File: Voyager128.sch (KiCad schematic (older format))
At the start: 22 parts, among them J1 AppleIIBus, U1 74HCT245, U2 621024, U3 GAL22V10, U4 74AHCT125

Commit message: Board done but ugly
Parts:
- removed U2: 621024, stdpads:SOP-32_P1.27mm, symbol GW_RAM:SRAM-128Kx8-SOP-32
- removed U3: GAL22V10, stdpads:PLCC-28, symbol GW_PLD:GAL22V10-PLCC
- removed U4: 74AHCT125, stdpads:SOIC-14_3.9mm, symbol 74xx:74LS125
- added C10, C11, C12, C13, C14, C15, C16, C7, C8, C9: 2u2, stdpads:C_0603, symbol Device:C_Small
- added U1: 621024, stdpads:TSOP-I-32_18.4x8mm_P0.5mm, symbol GW_RAM:SRAM-128Kx8-TSOP1-32
- added U10: 74LS32, stdpads:TSSOP-14_4.4x5mm_P0.65mm, symbol 74xx:74LS32
- added U11: 74AHC1G126GW, stdpads:SOT-353, symbol GW_Logic:741G126GW
- added U3, U4: 74LS174, stdpads:TSSOP-16_4.4x5mm_P0.65mm, symbol 74xx:74LS174
- added U5: 74LS04, stdpads:TSSOP-14_4.4x5mm_P0.65mm, symbol 74xx:74LS04
- added U6, U7, U8, U9: 74LS08, stdpads:TSSOP-14_4.4x5mm_P0.65mm, symbol 74xx:74LS08
- C2, C3, C4, C6: footprint stdpads:C_0805 -> stdpads:C_0603
- R1: value 1k -> 3k3
- U2: renamed from U1; footprint stdpads:SOIC-20W_7.5mm -> stdpads:TSSOP-20_4.4x6.5mm_P0.65mm
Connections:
- net labels added: ENWR1A0, INHOE, RCS, ~A0XOR1~, ~DEV~andA2, ~DEV~and~A2~
- net labels removed: R~CS~1, ~INH~b
- wire segments 120 -> 139
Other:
- note removed: "(1)"
- note removed: "(10)"
- note removed: "(11)"
- note removed: "(13)"
- note removed: "(14)"
- note removed: "(15)"
- note removed: "(16)"
- note removed: "(17)"
- note removed: "(18)"
- note removed: "(19)"
- note removed: "(2)"
- note removed: "(20)"
- note removed: "(21)"
- note removed: "(22)"
- note removed: "(23)"
- note removed: "(3)"
- note removed: "(4)"
- note removed: "(5)"
- note removed: "(6)"
- note removed: "(7)"
- note removed: "(8)"
- note removed: "(9)"
- moved on the sheet: C1, C2, C3, C4, C5, C6, FID1, FID2, FID3, FID4, FID5, H1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

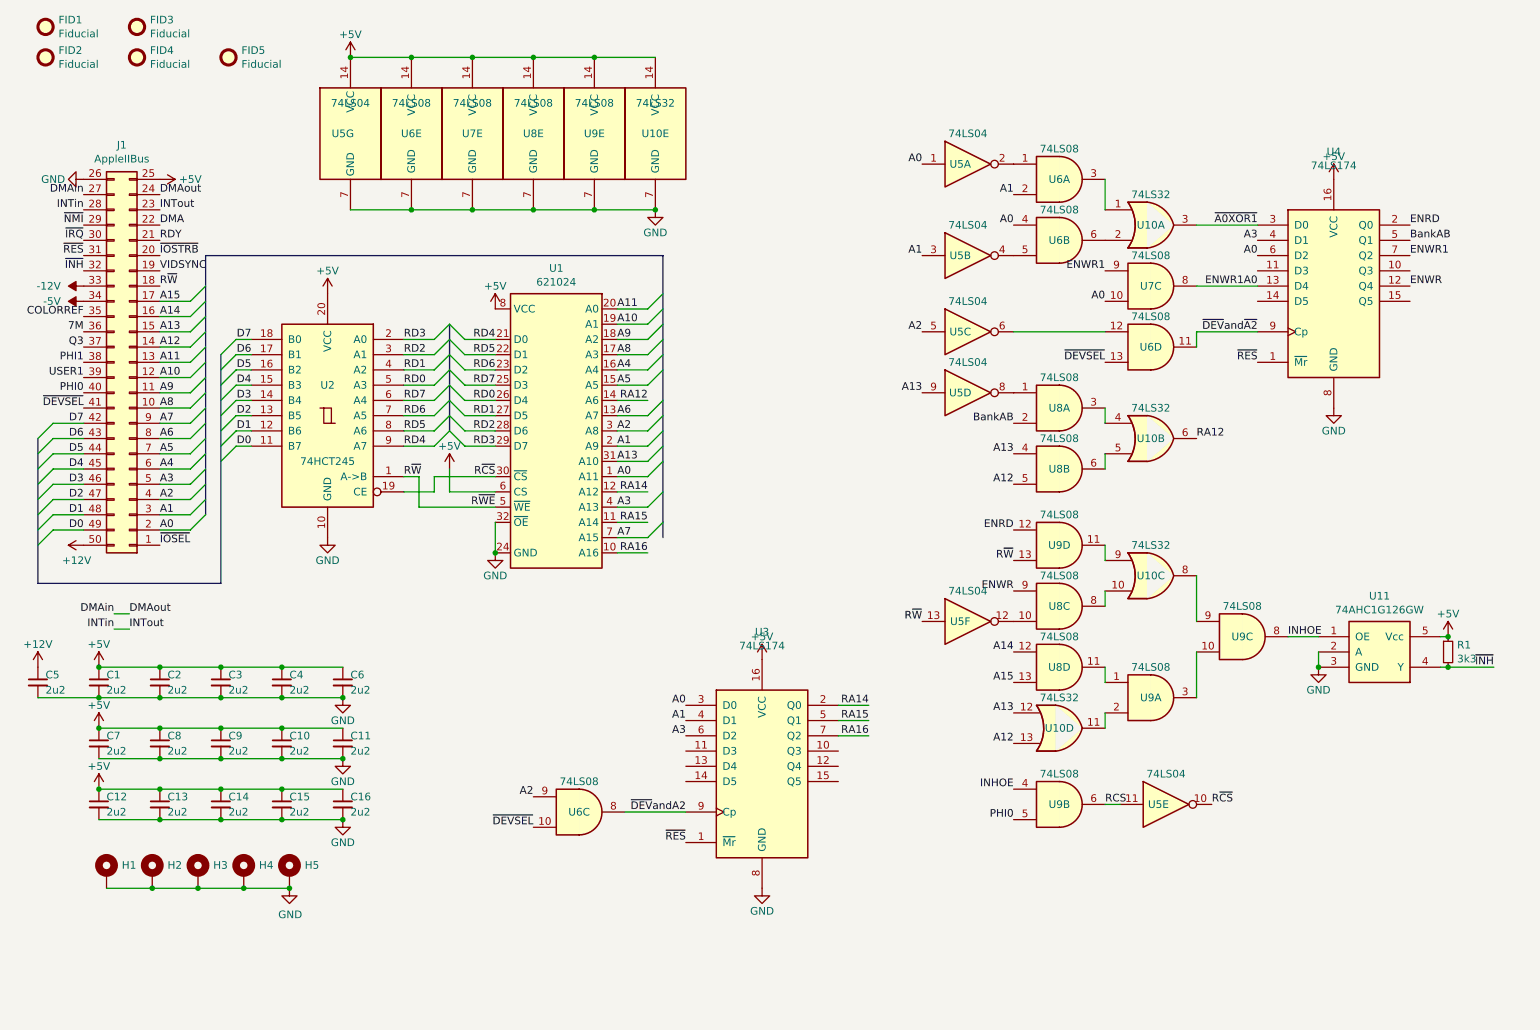
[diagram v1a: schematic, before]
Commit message: Routing done, needs made pretty
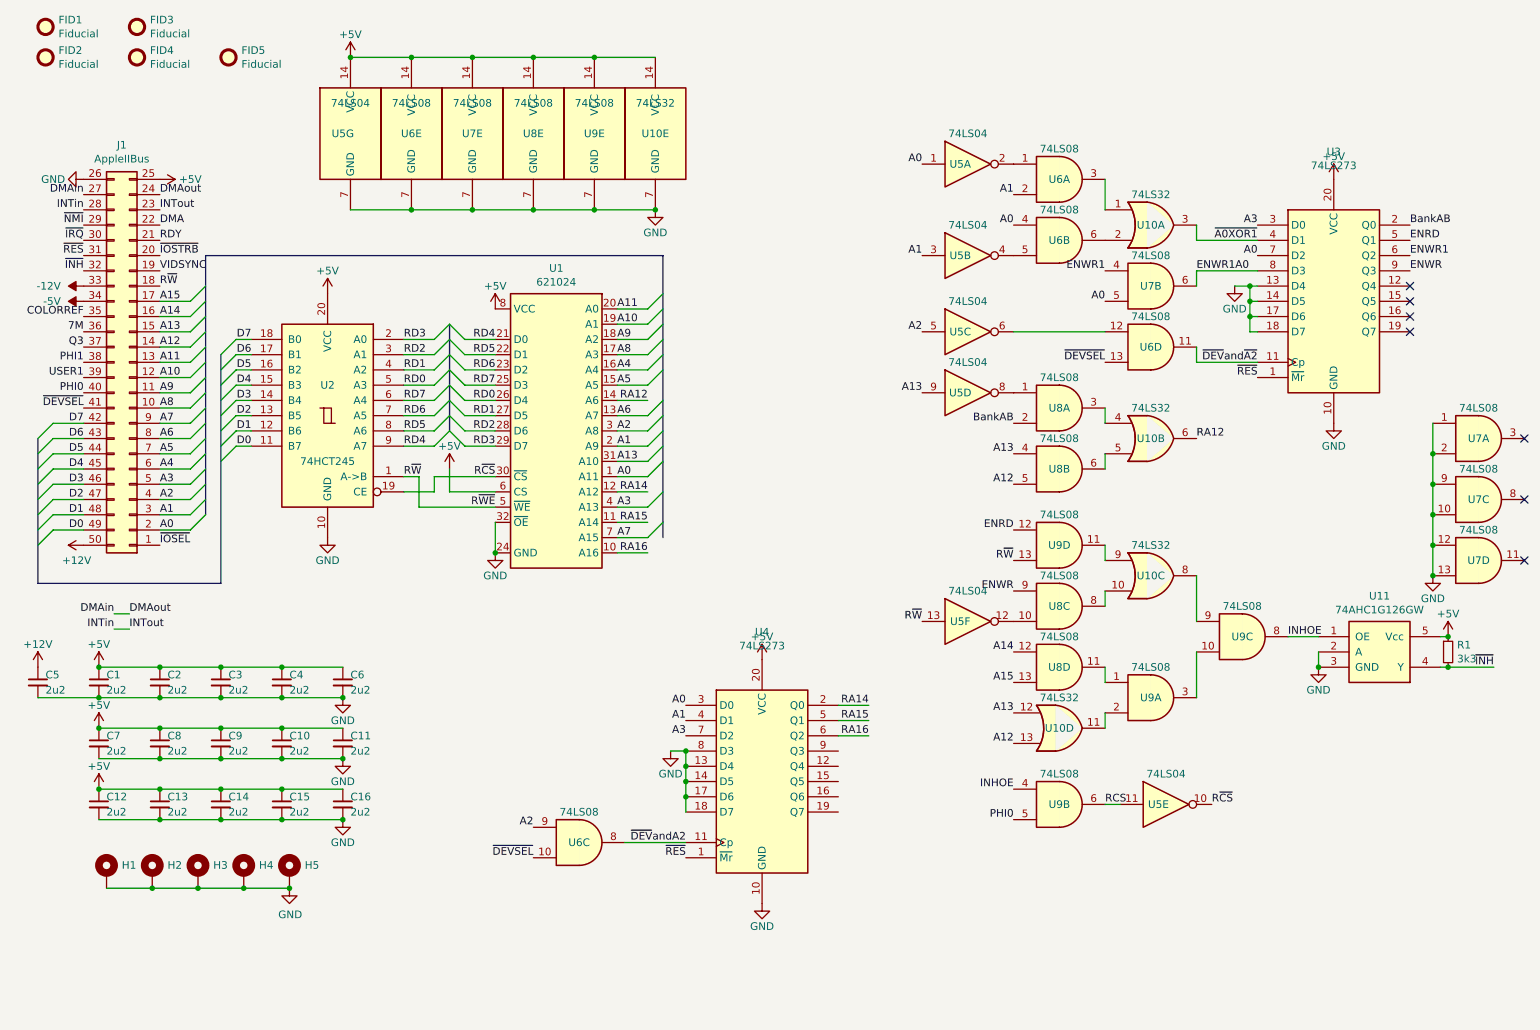
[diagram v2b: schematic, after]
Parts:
- removed U3, U4: 74LS174, stdpads:TSSOP-16_4.4x5mm_P0.65mm, symbol 74xx:74LS174
- added U3, U4: 74LS273, stdpads:TSSOP-20_4.4x6.5mm_P0.65mm, symbol 74xx:74LS273
- added unit 2 of U7
- added unit 3 of U7
- added unit 4 of U7
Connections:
- net +5V: now also U3.20 (VCC), U4.20 (VCC)
- net A0: now also U3.7 (D2), U4.3 (D0), U7.5; no longer U7.10
- net A1: now also U4.4 (D1)
- net A3: now also U3.3 (D0), U4.7 (D2)
- net BankAB: now also U3.2 (Q0)
- net ENRD: now also U3.5 (Q1)
- net ENWR: now also U3.9 (Q3)
- net ENWR1: now also U3.6 (Q2), U7.4; no longer U7.9
- net ENWR1A0: now also U3.8 (D3), U7.6; no longer U7.8
- net GND: now also U7.1, U7.2, U3.10 (GND), U3.13 (D4), U3.14 (D5), U3.17 (D6), U3.18 (D7), U4.10 (GND), U4.13 (D4), U4.14 (D5), U4.17 (D6), U4.18 (D7), U4.8 (D3), U7.10, U7.12, U7.13, U7.9
- net RA14: now also U4.2 (Q0)
- net RA15: now also U4.5 (Q1)
- net RA16: now also U4.6 (Q2)
- net ~A0XOR1~: now also U3.4 (D1)
- net ~DEV~andA2: now also U4.11 (Cp)
- net ~DEV~and~A2~: now also U3.11 (Cp)
- net ~RES~: now also U3.1 (~Mr), U4.1 (~Mr)
- no-connect marks 0 -> 7
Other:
- moved on the sheet: U6C
